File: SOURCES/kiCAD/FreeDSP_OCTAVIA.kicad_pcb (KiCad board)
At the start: 4 copper layers, 178 x 99 mm, 525 parts, among them IC1 TPS5430DDA, IC2 PCM1808QPWRQ1, J1 Conn_01x08, J10 Conn_01x02, J11 Conn_Coaxial, J12 IDC_2x5, J13 Conn_01x05, J16 RCJ-2223, J17 RCJ-2223, J2 DC7.5V-9V IN, J20 RCJ-2223, J21 RCJ-2223, J24 Conn_01x06, J25 Conn_01x06, J27 Conn_01x06, J28 Conn_01x06, J3 Conn_01x08, J4 Header_01x06, J5 RCJ-2223, J6 8P_DIP_SOCKET, J7 Header_01x04, J8 Header_01x04, J9 Conn_01x02, P1 Conn_02x20_Odd_Even, Q1 AO3401A, Q10 2SC3326, Q11 2SC3326, Q12 MJD45H11T4, Q13 2N7002, Q15 2SC3326, Q16 2SC3326, Q17 2SC3326, Q18 2SC3326, Q19 2SC3326, Q2 MMBT5401, Q20 2SC3326, Q21 2SC3326, Q22 2SC3326, Q23 2SC3326, Q24 2SC3326, Q25 2SC3326, Q26 2SC3326, Q27 2SC3326, Q28 2SC3326, Q29 AO3401A, Q3 2N7002, Q30 2N7002, Q31 2N7002, Q32 2N7002, Q4 MMBT5401, Q5 AO3401A, Q6 2N7002, Q7 AO3401A, Q8 2N7002, Q9 2N7002, SW1 SW_Push, SW2 SW_SPDT, SW3 SW_SPDT, SW4 SW_NOP_DPDT, SW7 DSP_RES, T1 PE-65612NL, U1 GP1UXC41QS, U10 74LVC1G86, U11 74LVC1G04, U12 ADAU1452, U13 25AA1024, U14 PCM5102A, U15 74LVC1G04, U16 PCM5102A, U17 PCM5102A, U18 PCM5102A, U2 PLR135-T10, U20 OPA1632DR, U21 OPA1632DR, U22 OPA1632DR, U23 OPA1632DR, U24 OPA1632DR, U25 OPA1632DR, U26 OPA1632DR, U27 OPA1632DR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

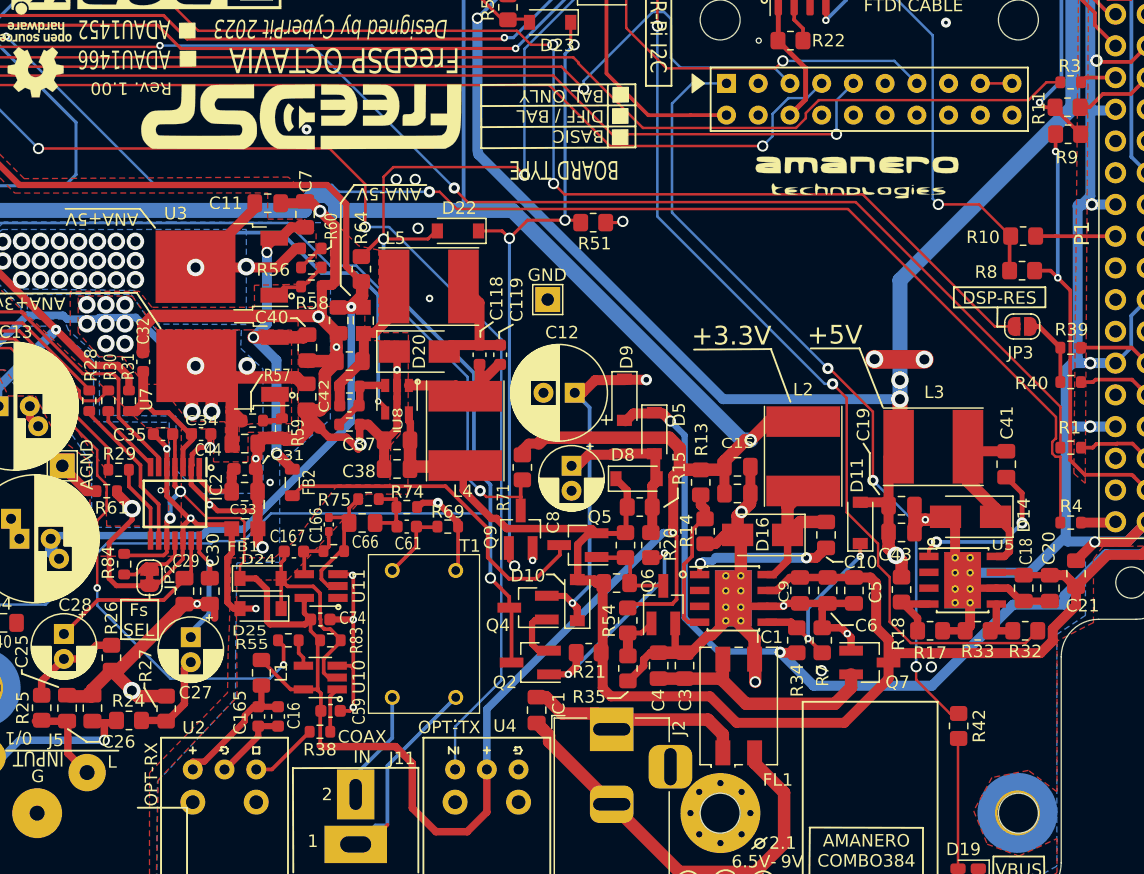
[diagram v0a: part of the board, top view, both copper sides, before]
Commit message: Fixed ACM9070F Land Patterns.
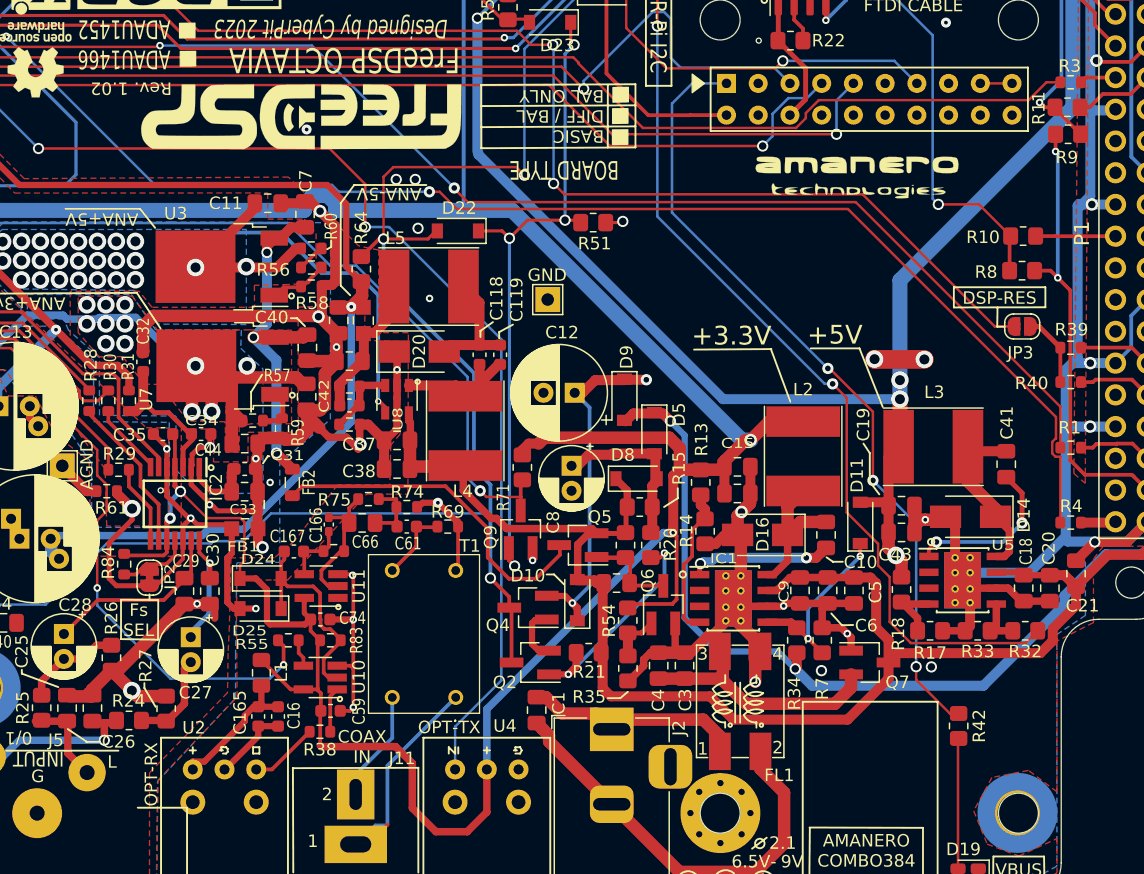
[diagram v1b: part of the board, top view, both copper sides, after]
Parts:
- FL1: value ACM9070 -> ACM9070F; footprint MyLibrary:ACM9070 -> MyLibrary:ACM9070F
- moved FL1 0.39 mm to (173.3, 134.1)
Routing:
- net GND: track 724.0 -> 724.7 mm
- net Net-(C3-Pad1): track 19.6 -> 20.2 mm
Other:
- board text added: "Rev. 1.02"
- board text removed: "Rev. 1.00"

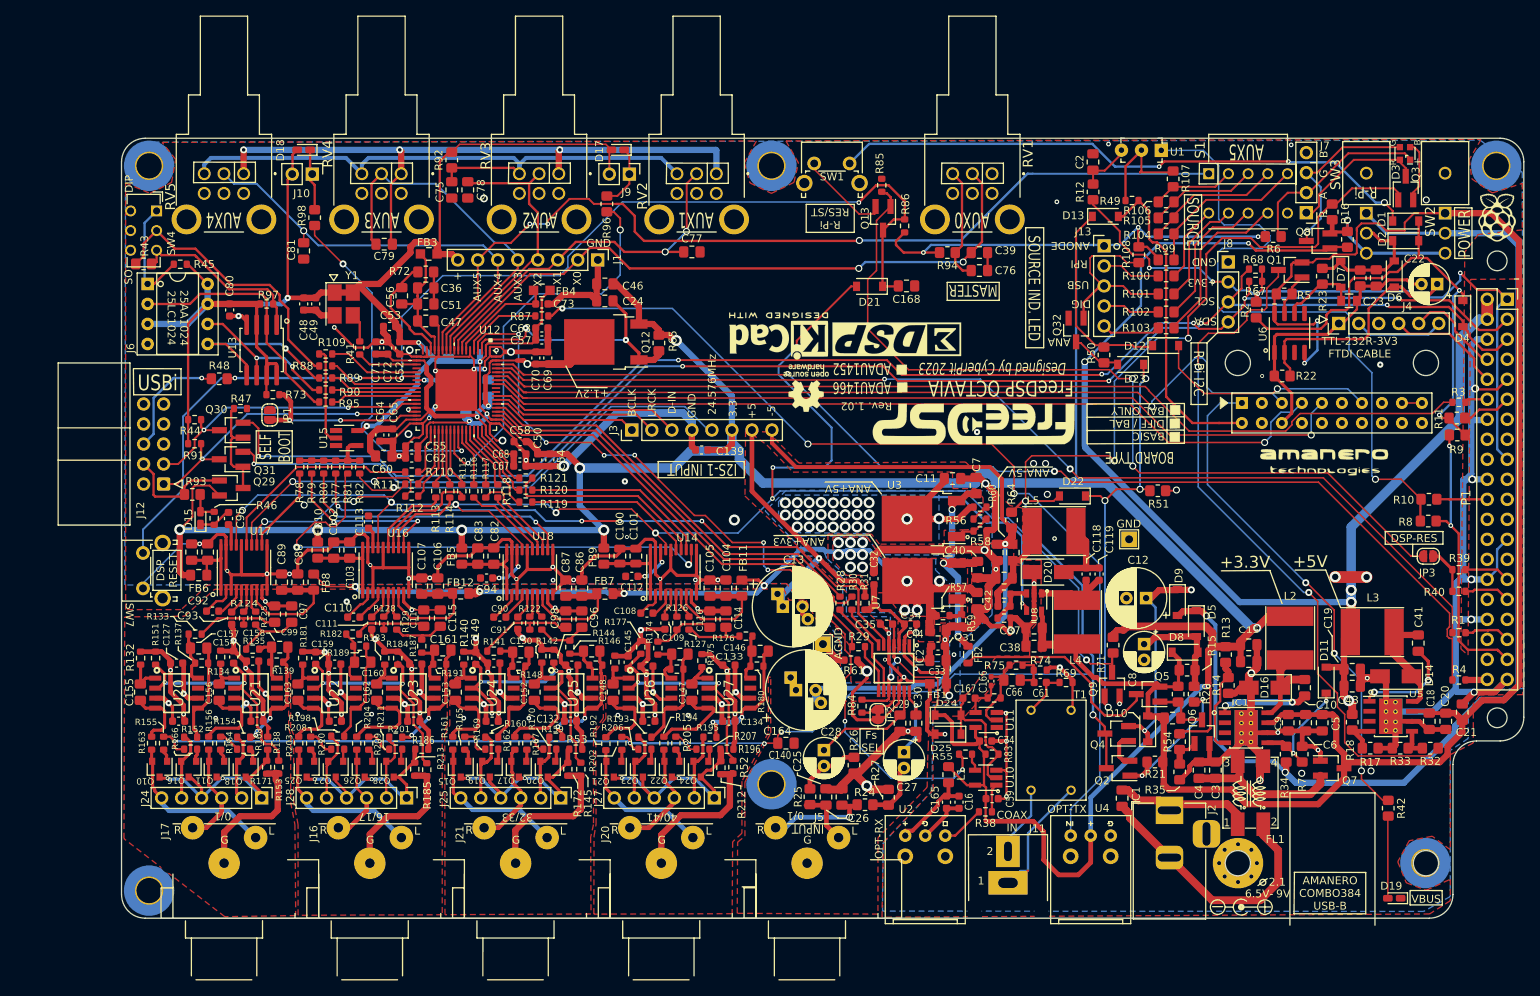
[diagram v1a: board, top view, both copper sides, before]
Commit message: Fixed ACM9070 lands. Selectable I2C for RPI/YORK
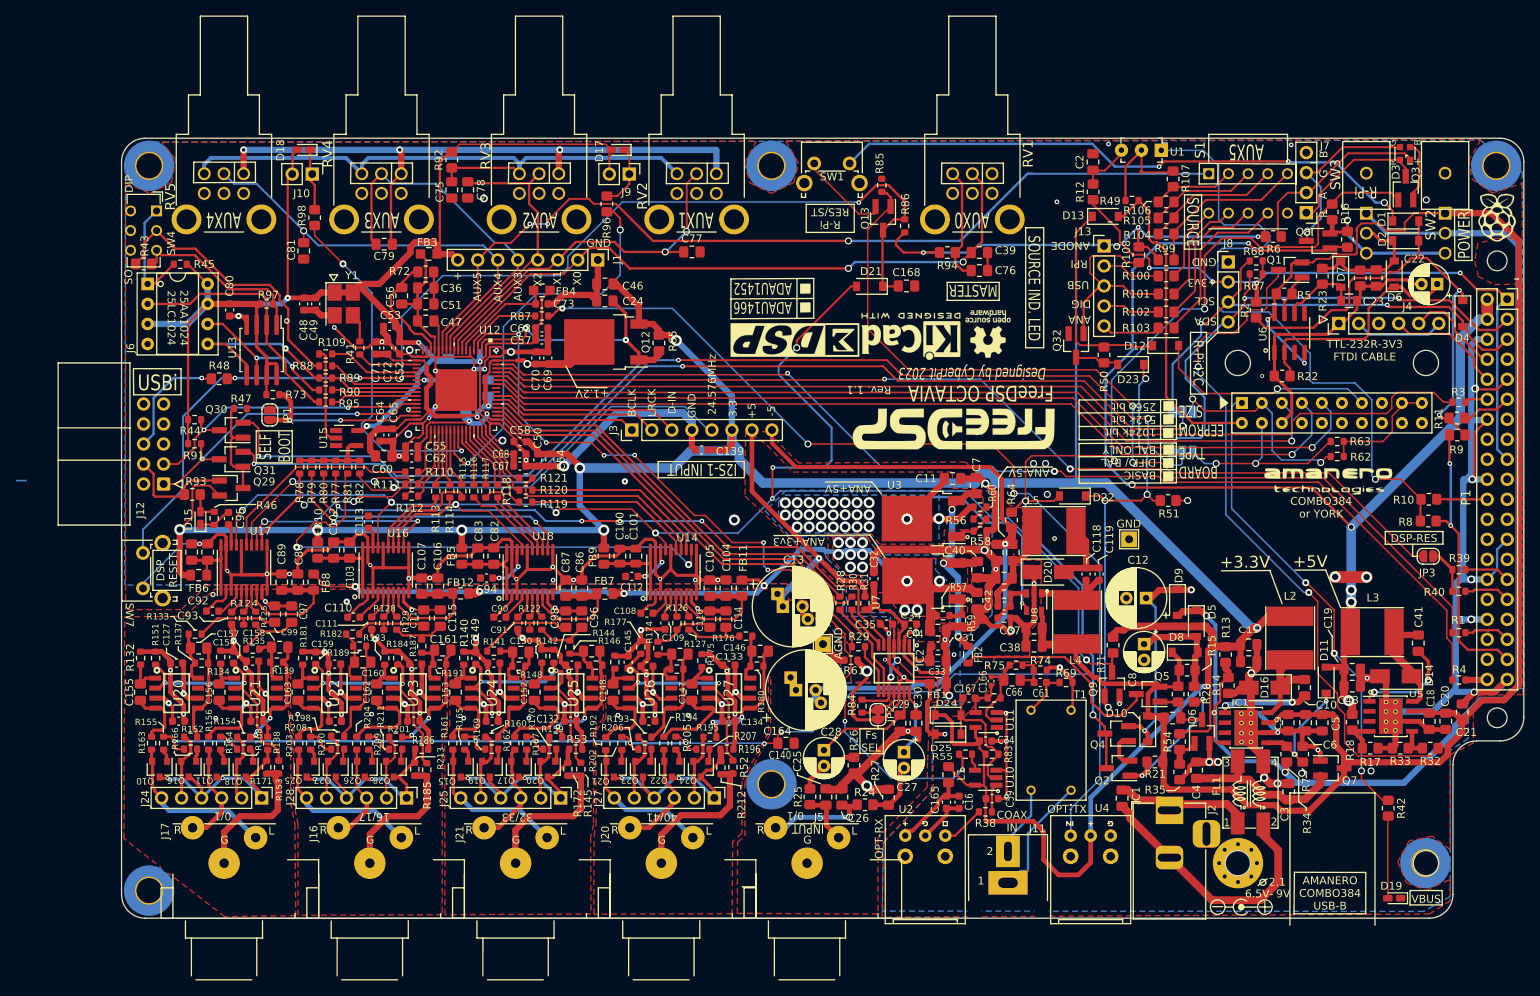
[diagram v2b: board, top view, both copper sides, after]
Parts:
- added JP4: SolderJumper_3_Bridged12, Jumper:SolderJumper-3_P1.3mm_Bridged12_Pad1.0x1.5mm_NumberLabels, B.Cu at (164.7, 90.8)
- added JP5: SolderJumper_3_Bridged12, Jumper:SolderJumper-3_P1.3mm_Bridged12_Pad1.0x1.5mm_NumberLabels, B.Cu at (164.7, 85.7)
- added R62: 2.2k, Resistor_SMD:R_0603_1608Metric, F.Cu at (184.3, 91.4)
- added R63: 2.2k, Resistor_SMD:R_0603_1608Metric, F.Cu at (184.3, 89.5)
- FL1: value ACM9070F -> ACM9070
- R57: value 180R -> 120R
- R59: value 270R -> 200R
- moved REF*** 24.1 mm to (140.0, 75.8)
- moved REF*** 16.8 mm to (130.2, 76.2)
- moved Z1 12.9 mm to (115.5, 76.6)
- moved C3 9.70 mm to (178.2, 133.9)
- moved LOGO1 2.62 mm to (135.7, 88.0)
- moved Z2 2.47 mm to (183.2, 94.5)
- moved Q32 1.97 mm to (151.2, 77.3)
- moved R51 1.81 mm to (162.8, 97.0)
- moved R68 1.04 mm to (174.0, 66.6)
- moved R67 0.95 mm to (174.0, 68.2)
- moved C4 0.31 mm to (166.5, 131.2)
- moved R7 0.06 mm to (179.9, 129.2)
- moved R34 0.06 mm to (177.9, 129.2)
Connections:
- net Net-(A1-Pad10) renamed +VSW
- A1 pad 12: Net-(A1-Pad12) -> AMA_SDA
- A1 pad 2: Net-(A1-Pad2) -> AMA_SCL
- Q30 pad 2: RP_SDA -> EX_SDA
- Q31 pad 2: RP_SCL -> EX_SCL
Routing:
- net EX_SDA: track 0.00 -> 139.1 mm, vias 0 -> 3
- net EX_SCL: track 0.00 -> 132.8 mm, vias 0 -> 3
- net RP_SCL: track 182.8 -> 63.2 mm, vias 5 -> 2
- net RP_SDA: track 182.4 -> 66.6 mm, vias 6 -> 2
- net AMA_SCL: track 0.00 -> 26.5 mm, vias 0 -> 2
- net AMA_SDA: track 0.00 -> 24.8 mm, vias 0 -> 2
- net +VSW: track 2.54 -> 15.4 mm
- net GND: track 724.7 -> 736.3 mm, vias 78 -> 80
- net +5V: track 160.6 -> 154.3 mm, vias 5 -> 6
- net BCK_IN2: track 108.5 -> 112.9 mm
- net Net-(A1-Pad1): track 63.8 -> 60.2 mm
- net /ALWAYS_ON: track 243.4 -> 239.8 mm
- net LRK_IN2: track 111.0 -> 114.2 mm
- net BCK_IN3: track 126.3 -> 129.1 mm
- net Net-(R10-Pad1): track 85.9 -> 83.4 mm
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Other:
- board text added: "1024k bit 512k bit 256k bit"
- board text added: "COMBO384 or YORK"
- board text added: "CONFIGURATION SELECT JUMPER"
- board text added: "EEPROM SIZE"
- board text added: "EXTRA I2S INPUT"
- board text added: "Rev. 1.1"
- board text added: "YORK"
- board text added: "~POS-1"
- board text added: "~POS-2"
- board text added: "~POS-3"
- board text added: "~POS-4"
- board text removed: "POS-1"
- board text removed: "POS-2"
- board text removed: "POS-3"
- board text removed: "POS-4"
- board text removed: "Rev. 1.02"

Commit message: A method of board type convertion had changed.
Add an AGND fill on the bottom layer. The connection path for the Standard type board had changed. No features/functions changed.
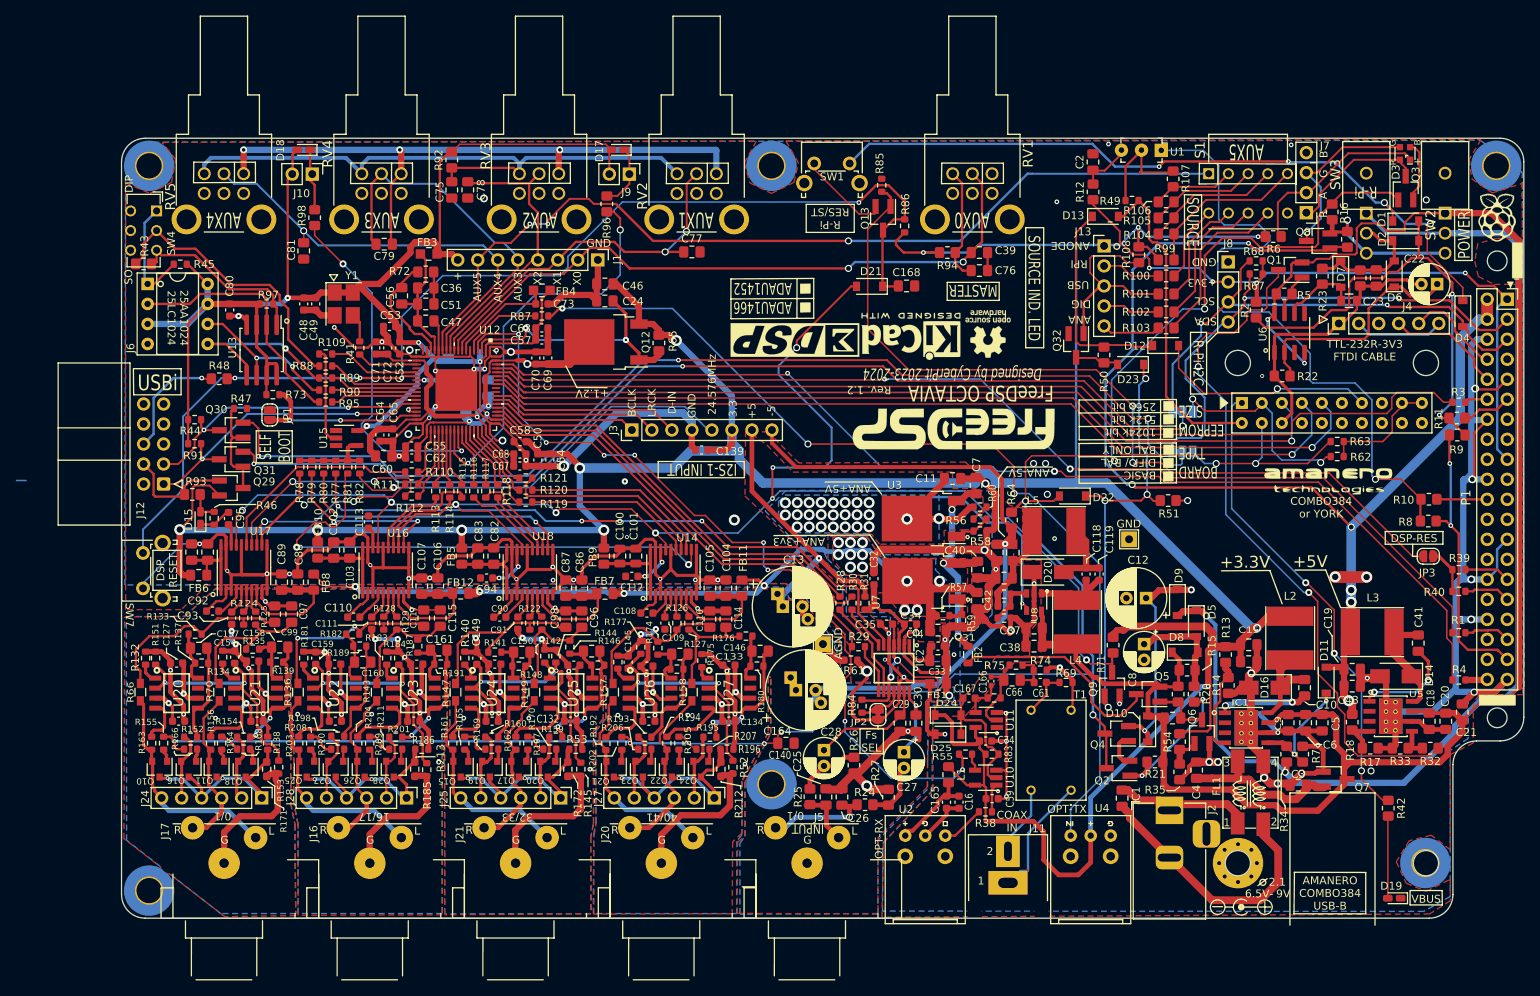
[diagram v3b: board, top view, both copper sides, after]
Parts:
- removed C147, C148, C152, C153, C155, C156, C162, C163: NOP, Capacitor_SMD:C_0805_2012Metric_Pad1.18x1.45mm_HandSolder
- added R136: NOP, Resistors_SMD:R_0603_HandSoldering, F.Cu at (52.4, 121.3)
- added R143: NOP, Resistors_SMD:R_0603_HandSoldering, F.Cu at (62.4, 121.3)
- added R147: NOP, Resistors_SMD:R_0603_HandSoldering, F.Cu at (72.4, 121.3)
- added R149: NOP, Resistors_SMD:R_0603_HandSoldering, F.Cu at (82.4, 121.3)
- added R157: NOP, Resistors_SMD:R_0603_HandSoldering, F.Cu at (92.4, 121.3)
- added R158: NOP, Resistors_SMD:R_0603_HandSoldering, F.Cu at (102.4, 121.3)
- added R66: NOP, Resistors_SMD:R_0603_HandSoldering, F.Cu at (32.4, 121.3)
- added R70: NOP, Resistors_SMD:R_0603_HandSoldering, F.Cu at (42.4, 121.3)
- R171, R172, R212, R213: footprint Resistor_SMD:R_0603_1608Metric -> Resistor_SMD:R_0603_1608Metric_Pad0.98x0.95mm_HandSolder
- moved C3 1.46 mm to (179.4, 133.1), turned to 180 degrees
- moved Q7 1.45 mm to (184.1, 132.4)
- moved R132 0.63 mm to (33.1, 117.0)
- moved C161 0.51 mm to (70.3, 116.0)
- moved R187 0.51 mm to (67.6, 115.5)
- moved R142 0.38 mm to (83.7, 116.7)
- moved R173 0.38 mm to (93.0, 117.5)
- moved R205 0.38 mm to (100.7, 127.8)
- moved R194 0.38 mm to (99.2, 127.8)
- moved R171 0.25 mm to (48.4, 131.1)
- moved C131 0.25 mm to (87.4, 117.9)
- moved R134 0.25 mm to (42.8, 116.9)
- moved R144 0.25 mm to (85.1, 116.7)
- moved R150 0.25 mm to (90.5, 117.9)
- moved R156 0.25 mm to (41.3, 127.8)
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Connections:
- D4 pad 1: /~RASPI_OFF -> Net-(D1-Pad1)
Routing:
- net Net-(D1-Pad1): track 75.5 -> 94.2 mm, vias 3 -> 4
- net /ADC_IO Part/DAC/DAC1_L: track 10.1 -> 25.4 mm, vias 0 -> 2
- net /ADC_IO Part/DAC/DAC0_L: track 11.2 -> 25.7 mm
- net /ADC_IO Part/DAC/DAC3_L: track 8.00 -> 20.0 mm
- net /ADC_IO Part/DAC/DAC2_L: track 12.7 -> 24.4 mm
- net /ADC_IO Part/DAC/DAC0_R: track 8.52 -> 19.0 mm
- net /ADC_IO Part/DAC/OUT41_P: track 14.4 -> 22.7 mm
- net /ADC_IO Part/DAC/OUT33_P: track 14.2 -> 22.4 mm
- net /ADC_IO Part/DAC/DAC1_R: track 6.99 -> 15.1 mm
- net /ADC_IO Part/DAC/OUT17_P: track 12.9 -> 20.8 mm
- net /ADC_IO Part/DAC/OUT1_P: track 13.9 -> 21.7 mm
- net /ADC_IO Part/DAC/DAC2_R: track 6.28 -> 13.8 mm
- net GND: track 736.3 -> 743.6 mm
- net /ADC_IO Part/DAC/OUT40_P: track 18.8 -> 26.0 mm
- net /ADC_IO Part/DAC/OUT32_P: track 19.7 -> 26.9 mm
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- added copper zone on B.Cu, net GNDA
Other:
- board text added: "Designed by CyberPit 2023-2024"
- board text added: "EXTRA I2S-1 INPUT"
- board text added: "Rev. 1.2"
- board text removed: "Designed by CyberPit 2023"
- board text removed: "EXTRA I2S INPUT"
- board text removed: "Rev. 1.1"
